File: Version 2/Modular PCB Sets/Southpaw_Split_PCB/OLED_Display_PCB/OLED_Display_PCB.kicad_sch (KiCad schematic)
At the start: 2 parts, among them SW1 RotaryEncoder_Switch

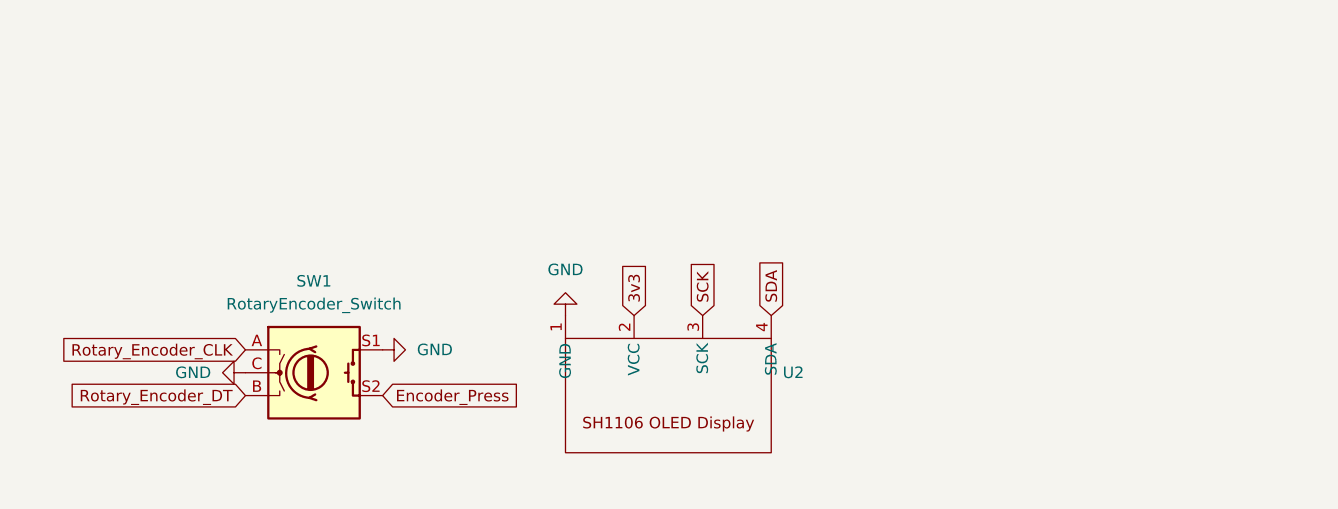
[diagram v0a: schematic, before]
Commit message: rework for schematic structure to accomodate new pico symbol and jst connectors
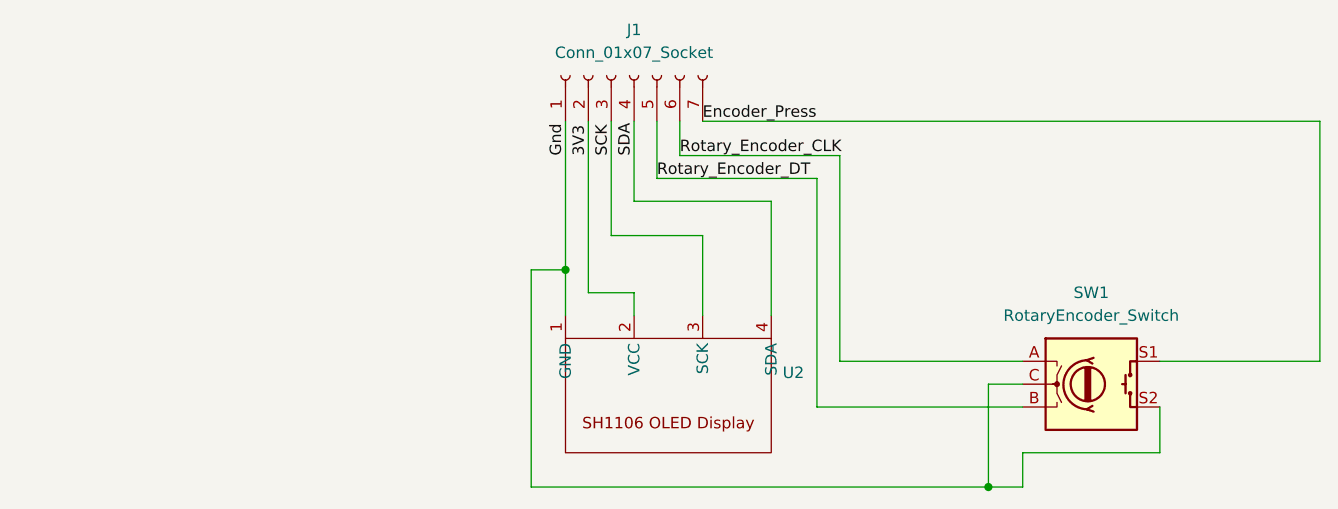
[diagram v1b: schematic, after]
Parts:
- added J1: Conn_01x07_Socket, Connector_JST:JST_PH_B7B-PH-K_1x07_P2.00mm_Vertical, symbol Connector:Conn_01x07_Socket
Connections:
- net Encoder_Press: now also SW1.S1, J1.7 (Pin_7); no longer SW1.S2
- net Rotary_Encoder_CLK: now also J1.6 (Pin_6)
- net Rotary_Encoder_DT: now also J1.5 (Pin_5)
- net SCK: now also J1.3 (Pin_3)
- net SDA: now also J1.4 (Pin_4)
- net 3v3 renamed 3V3
- net 3V3: now also J1.2 (Pin_2)
- net GND renamed Gnd
- net Gnd: now also SW1.S2, J1.1 (Pin_1); no longer SW1.S1
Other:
- moved on the sheet: SW1

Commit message: created footprints for all lockout and oled display
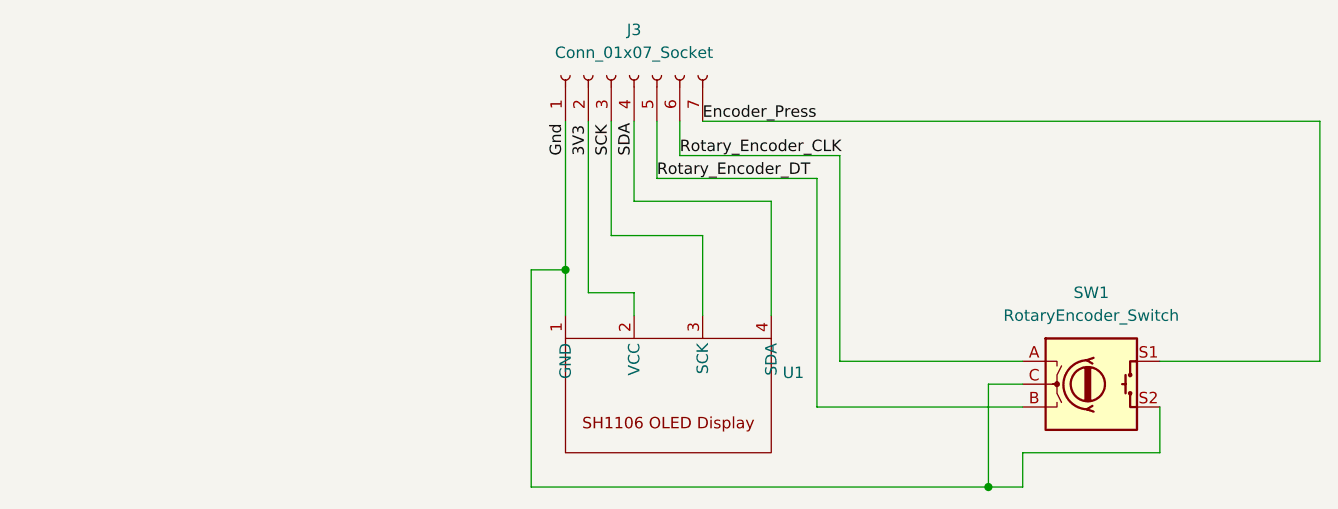
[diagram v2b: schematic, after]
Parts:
- U1: renamed from U2; footprint (none) -> Wilson's_Footprint_Library:Hosyond SH1106 OLED Display
- renumbered J1 to J3
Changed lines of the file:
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@@
 		(dnp no)
 		(fields_autoplaced yes)
-		(property "Reference" "U2"
+		(property "Reference" "U1"
 			(at 166.37 87.6299 0)
 			(effects
@@
 			)
 		)
-		(property "Footprint" ""
+		(property "Footprint" "Wilson's_Footprint_Library:Hosyond SH1106 OLED Display"
 			(at 142.24 83.82 0)
 			(effects
@@
 		)
 		(instances
+			(project "Southpaw_Split_PCB"
+				(path "/12c03e98-16e3-4861-a1ce-d2b4d8ad36ee/0e181ba1-7794-44cb-ad32-5d32438b070a"
+					(reference "U1")
+					(unit 1)
+				)
+			)
 			(project "OLED_Display_PCB"
 				(path "/b5d6275e-4442-4422-957c-10e43bae2dcb"
@@
 		)
 		(instances
+			(project "Southpaw_Split_PCB"
+				(path "/12c03e98-16e3-4861-a1ce-d2b4d8ad36ee/0e181ba1-7794-44cb-ad32-5d32438b070a"
+					(reference "SW1")
+					(unit 1)
+				)
+			)
 			(project "OLED_Display_PCB"
 				(path "/b5d6275e-4442-4422-957c-10e43bae2dcb"
@@
 		(dnp no)
 		(fields_autoplaced yes)
-		(property "Reference" "J1"
+		(property "Reference" "J3"
 			(at 149.86 49.53 90)
 			(effects
@@
 		)
 		(instances
+			(project "Southpaw_Split_PCB"
+				(path "/12c03e98-16e3-4861-a1ce-d2b4d8ad36ee/0e181ba1-7794-44cb-ad32-5d32438b070a"
+					(reference "J3")
+					(unit 1)
+				)
+			)
 			(project ""
 				(path "/b5d6275e-4442-4422-957c-10e43bae2dcb"

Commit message: general part layout
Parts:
- renumbered U1 to OLED1, SW1 to RotarySW1
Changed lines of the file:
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@@
 		(dnp no)
 		(fields_autoplaced yes)
-		(property "Reference" "U1"
+		(property "Reference" "OLED1"
 			(at 166.37 87.6299 0)
 			(effects
@@
 			(project "Southpaw_Split_PCB"
 				(path "/12c03e98-16e3-4861-a1ce-d2b4d8ad36ee/0e181ba1-7794-44cb-ad32-5d32438b070a"
-					(reference "U1")
+					(reference "OLED1")
 					(unit 1)
 				)
@@
 			(project "OLED_Display_PCB"
 				(path "/b5d6275e-4442-4422-957c-10e43bae2dcb"
-					(reference "U2")
+					(reference "OLED1")
 					(unit 1)
 				)
@@
 		(dnp no)
 		(fields_autoplaced yes)
-		(property "Reference" "SW1"
+		(property "Reference" "RotarySW1"
 			(at 200.66 78.74 0)
 			(effects
@@
 			(project "Southpaw_Split_PCB"
 				(path "/12c03e98-16e3-4861-a1ce-d2b4d8ad36ee/0e181ba1-7794-44cb-ad32-5d32438b070a"
-					(reference "SW1")
+					(reference "RotarySW1")
 					(unit 1)
 				)
@@
 			(project "OLED_Display_PCB"
 				(path "/b5d6275e-4442-4422-957c-10e43bae2dcb"
-					(reference "SW1")
+					(reference "RotarySW1")
 					(unit 1)
 				)
@@
 			(project ""
 				(path "/b5d6275e-4442-4422-957c-10e43bae2dcb"
-					(reference "J1")
-					(unit 1)
-				)
+					(reference "J3")
+					(unit 1)
+				)
